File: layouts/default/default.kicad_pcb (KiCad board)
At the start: 2 copper layers, 39 x 17 mm, 13 parts

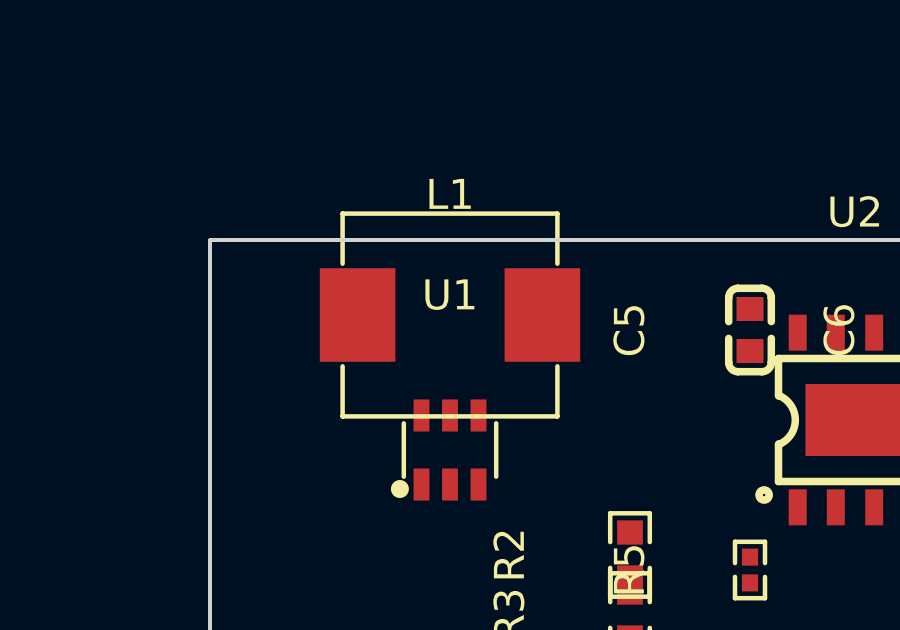
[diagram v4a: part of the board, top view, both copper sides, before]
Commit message: Use compact 4x4x2mm inductor (SMNR4020-22UH)
Replaced bulky 7.3x6.6x3mm inductor with 4x4x2mm shielded version.
Same 22µH value, 1.05A rated - sufficient for Pi Zero 2W load.
Max component height now 2.1mm (SS34 Schottky diode).
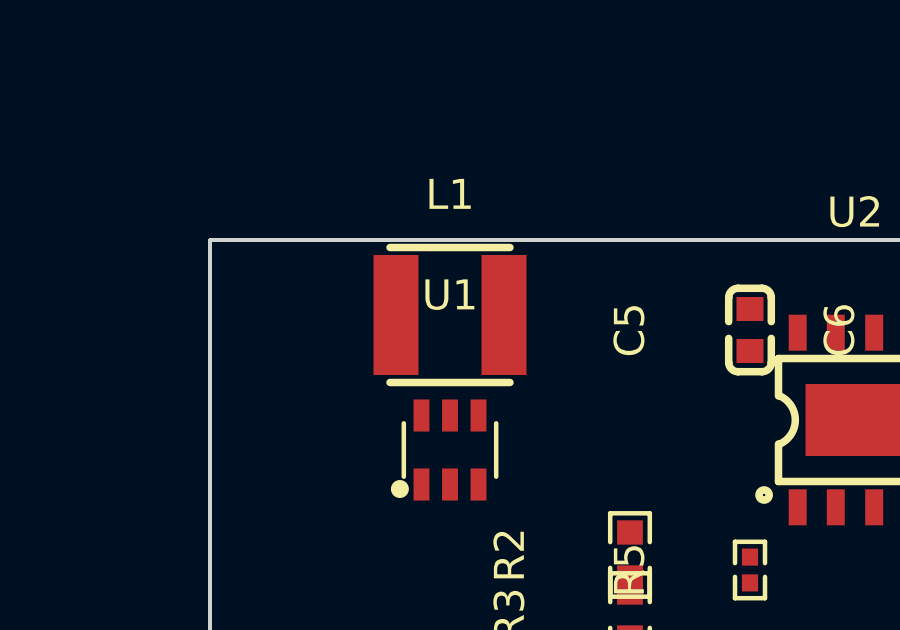
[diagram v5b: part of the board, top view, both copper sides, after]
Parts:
- L1: value L 0H -> (none); footprint SXN_SMMS0630_220M:IND-SMD_L7.3-W6.6_MHCI06030 -> SXN_SMNR4020_22UH:IND-SMD_L4.0-W4.0_LQH44PN2R2MP0L
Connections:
- D1 pad 2: A -> 2
- L1 pad 1: hv -> 2
- L1 pad 2: A -> hv
- U1 pad 1: A -> 2
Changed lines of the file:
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@@
 	(net 14 "c_out-power-hv")
 	(net 15 "lv")
-	(net 1 "A")
+	(net 1 "2")
 	(net 3 "hv")
 	(net 4 "FB")
@@
 			(size 0.53 1.07)
 			(layers "F.Cu" "F.Paste" "F.Mask")
-			(net 1 "A")
+			(net 1 "2")
 		)
 		(pad "2" smd rect
@@
 		)
 	)
-	(footprint "SXN_SMMS0630_220M:IND-SMD_L7.3-W6.6_MHCI06030"
+	(footprint "SXN_SMNR4020_22UH:IND-SMD_L4.0-W4.0_LQH44PN2R2MP0L"
 		(layer "F.Cu")
 		(at 107 82.5)
@@
 			)
 		)
-		(property "Value" "L 0H"
+		(property "Value" ""
 			(at 0 4)
 			(layer "F.Fab")
@@
 			)
 		)
-		(property "LCSC" "C128694"
-			(at 0 0 0)
-			(layer "User.9")
-			(hide yes)
-		)
-		(property "Manufacturer" "SXN(Shun Xiang Nuo Elec)"
+		(property "LCSC" "C135264"
+			(at 0 0 0)
+			(layer "User.9")
+			(hide yes)
+		)
+		(property "Manufacturer" "SXN"
 			(at 0 0 0)
 			(layer "User.9")
@@
 			(hide yes)
 		)
-		(property "Partnumber" "SMMS0630-220M"
-			(at 0 0 0)
-			(layer "User.9")
-			(hide yes)
-		)
-		(property "Datasheet" "https://www.lcsc.com/datasheet/lcsc_datasheet_2108131530_SXN-Shun-Xiang-Nuo-Elec-SMMS0630-220M_C128694.pdf"
+		(property "Partnumber" "SMNR4020-22UH"
+			(at 0 0 0)
+			(layer "User.9")
+			(hide yes)
+		)
+		(property "Datasheet" "https://www.lcsc.com/datasheet/lcsc_datasheet_2108131530_SXN-Shun-Xiang-Nuo-Elec-SMNR4020-22UH_C135264.pdf"
 			(at 0 0 0)
 			(layer "User.9")
@@
 			(hide yes)
 		)
-		(property "lcsc_id" "C128694"
+		(property "lcsc_id" "C135264"
 			(at 0 0 0)
 			(layer "User.9")
@@
 		(attr smd)
 		(fp_line
-			(start -3.58 -1.71)
-			(end -3.58 -3.38)
-			(stroke
-				(width 0.15)
-				(type solid)
-			)
-			(layer "F.SilkS")
-			(layers "F.SilkS")
-			(locked no)
-		)
-		(fp_line
-			(start -3.58 -3.38)
-			(end 3.58 -3.38)
-			(stroke
-				(width 0.15)
-				(type solid)
-			)
-			(layer "F.SilkS")
-			(layers "F.SilkS")
-			(locked no)
-		)
-		(fp_line
-			(start 3.58 -3.38)
-			(end 3.58 -1.71)
-			(stroke
-				(width 0.15)
-				(type solid)
-			)
-			(layer "F.SilkS")
-			(layers "F.SilkS")
-			(locked no)
-		)
-		(fp_line
-			(start -3.58 1.71)
-			(end -3.58 3.38)
-			(stroke
-				(width 0.15)
-				(type solid)
-			)
-			(layer "F.SilkS")
-			(layers "F.SilkS")
-			(locked no)
-		)
-		(fp_line
-			(start -3.58 3.38)
-			(end 3.58 3.38)
-			(stroke
-				(width 0.15)
-				(type solid)
-			)
-			(layer "F.SilkS")
-			(layers "F.SilkS")
-			(locked no)
-		)
-		(fp_line
-			(start 3.58 3.38)
-			(end 3.58 1.71)
-			(stroke
-				(width 0.15)
+			(start -2 -2.25)
+			(end 2 -2.25)
+			(stroke
+				(width 0.25)
+				(type solid)
+			)
+			(layer "F.SilkS")
+			(layers "F.SilkS")
+			(locked no)
+		)
+		(fp_line
+			(start -2 2.25)
+			(end 2 2.25)
+			(stroke
+				(width 0.25)
 				(type solid)
 			)
@@
 		)
 		(fp_circle
-			(center -3.55 3.31)
-			(end -3.52 3.31)
+			(center -2 2)
+			(end -1.97 2)
 			(stroke
 				(width 0.06)
@@
 			)
 		)
+		(pad "1" smd rect
+			(at -1.8 0 0)
+			(size 1.5 4)
+			(layers "F.Cu" "F.Paste" "F.Mask")
+			(net 1 "2")
+		)
 		(pad "2" smd rect
-			(at 3.08 0 0)
-			(size 2.52 3.12)
-			(layers "F.Cu" "F.Paste" "F.Mask")
-			(net 1 "A")
-		)
-		(pad "1" smd rect
-			(at -3.08 0 0)
-			(size 2.52 3.12)
+			(at 1.8 0 0)
+			(size 1.5 4)
 			(layers "F.Cu" "F.Paste" "F.Mask")
 			(net 3 "hv")
 		)
 		(embedded_fonts no)
-		(model "${KIPRJMOD}/../../parts/SXN_SMMS0630_220M/IND-SMD_L7.1-W6.6-H2.8.step"
+		(model "${KIPRJMOD}/../../parts/SXN_SMNR4020_22UH/IND-SMD_L4.0-W4.0-H1.65.STEP"
 			(offset
 				(xyz 0 0 -0)
@@
 			(size 2 2)
 			(layers "F.Cu" "F.Paste" "F.Mask")
-			(net 1 "A")
+			(net 1 "2")
 		)
 		(pad "1" smd rect

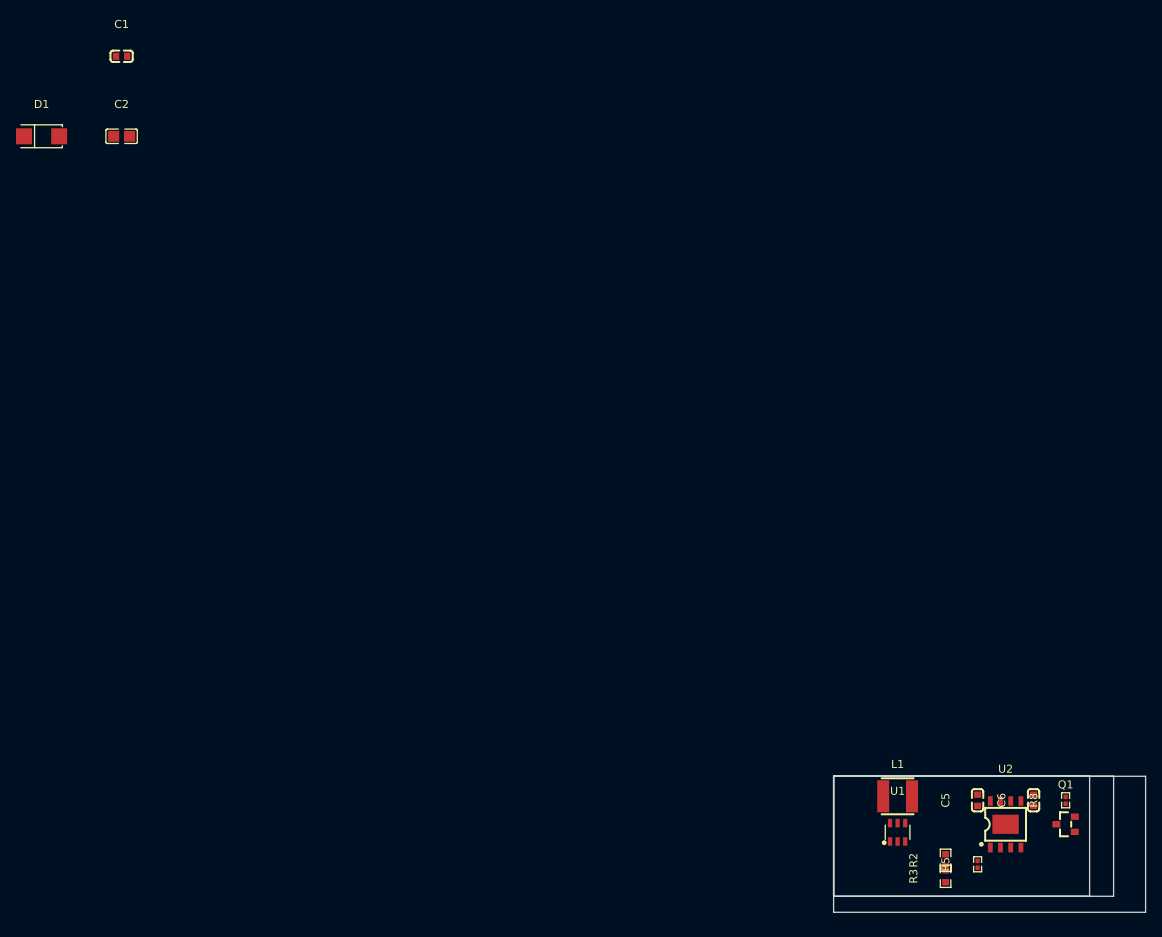
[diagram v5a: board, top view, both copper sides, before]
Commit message: Add PCB layout: 6 solder pads, component placement, routing, ground pour
- Created SolderPad component (2x1.5mm SMD pads) for 6 wire connections
- Board outline: 30x18mm with rounded corners
- 3-zone layout: charger (left) → MOSFET (center) → boost (right)
- Solder pads along bottom edge: VUSB, GND, VBAT, PI_EN, V5_PI, CHG
- 50 trace segments, 11 vias, GND pour on B.Cu
- Power traces 0.5mm, signal traces 0.25mm
- Silkscreen labels for all pads, board title NW-PWR
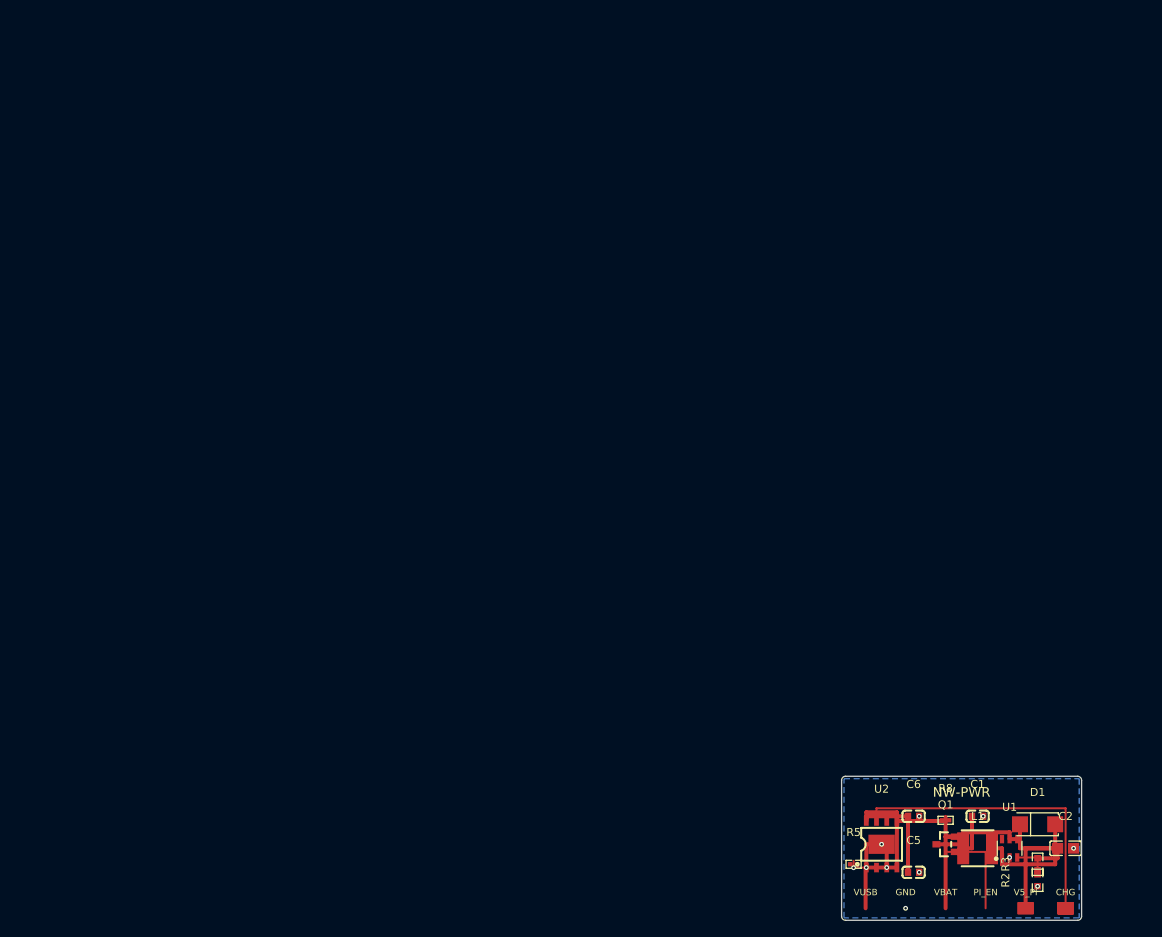
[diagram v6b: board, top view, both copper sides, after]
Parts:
- added J1, J3, J4, J5: , SolderPad:SolderPad, F.Cu at (128.0, 96.5)
- added J2, J6: , SolderPad:SolderPad, F.Cu at (123.0, 96.5)
- moved D1 151.3 mm to (124.5, 86.0)
- moved C2 147.8 mm to (128.0, 89.0)
- moved C1 143.1 mm to (117.0, 85.0)
- moved U2 15.7 mm to (105.0, 88.5)
- moved R5 15.5 mm to (101.5, 91.0), turned to 0 degrees
- moved Q1 15.2 mm to (113.0, 88.5)
- moved R8 15.2 mm to (113.0, 85.5), turned to 0 degrees
- moved C6 15.1 mm to (109.0, 85.0), turned to 0 degrees
- moved U1 14.1 mm to (121.0, 89.0)
- moved C5 12.0 mm to (109.0, 92.0), turned to 0 degrees
- moved L1 11.9 mm to (117.0, 89.0)
- moved R2 11.8 mm to (124.5, 93.0)
- moved R3 11.6 mm to (124.5, 91.0)
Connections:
- L1 pad 1: 2 -> hv
- L1 pad 2: hv -> 2
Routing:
- net chg_stat: track 0.00 -> 37.7 mm
- net c_in-power-hv: track 0.00 -> 26.6 mm
- net c_bat-power-hv: track 0.00 -> 26.2 mm
- net c_out-power-hv: track 0.00 -> 23.0 mm
- net hv: track 0.00 -> 18.5 mm
- net pi_en: track 0.00 -> 15.6 mm
- net 2: track 0.00 -> 14.9 mm
- net lv: track 0.00 -> 8.37 mm, vias 0 -> 11
- net FB: track 0.00 -> 4.65 mm
- net PROG: track 0.00 -> 3.70 mm
- added copper zone on B.Cu, net lv
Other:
- board size 39 x 17 mm -> 30 x 18 mm
- board text added: "CHG"
- board text added: "GND"
- board text added: "NW-PWR"
- board text added: "PI_EN"
- board text added: "V5_PI"
- board text added: "VBAT"
- board text added: "VUSB"

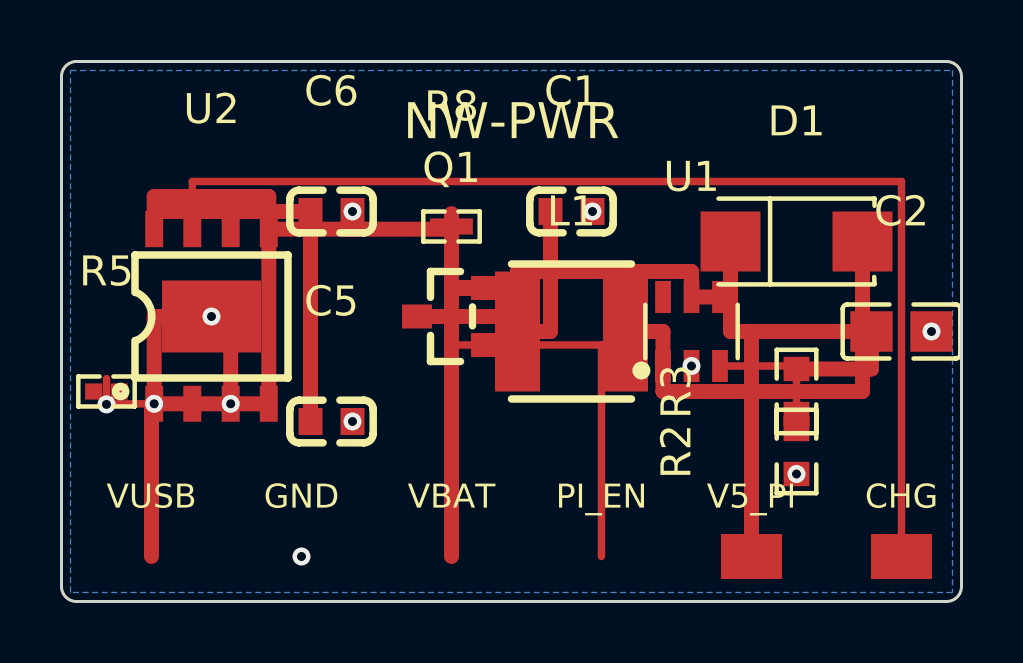
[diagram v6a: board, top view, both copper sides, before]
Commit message: Fix layout: proper pad spacing, clean placement, remove bad routing
- 6 solder pads evenly spaced along bottom edge (4.8mm apart)
- Components grouped: charger left, MOSFET center, boost right
- Removed all programmatic traces/vias/zones - route in KiCad
- Clean silkscreen labels (VUSB, GND, VBAT, EN, 5V, CHG)
- 30x18mm board outline
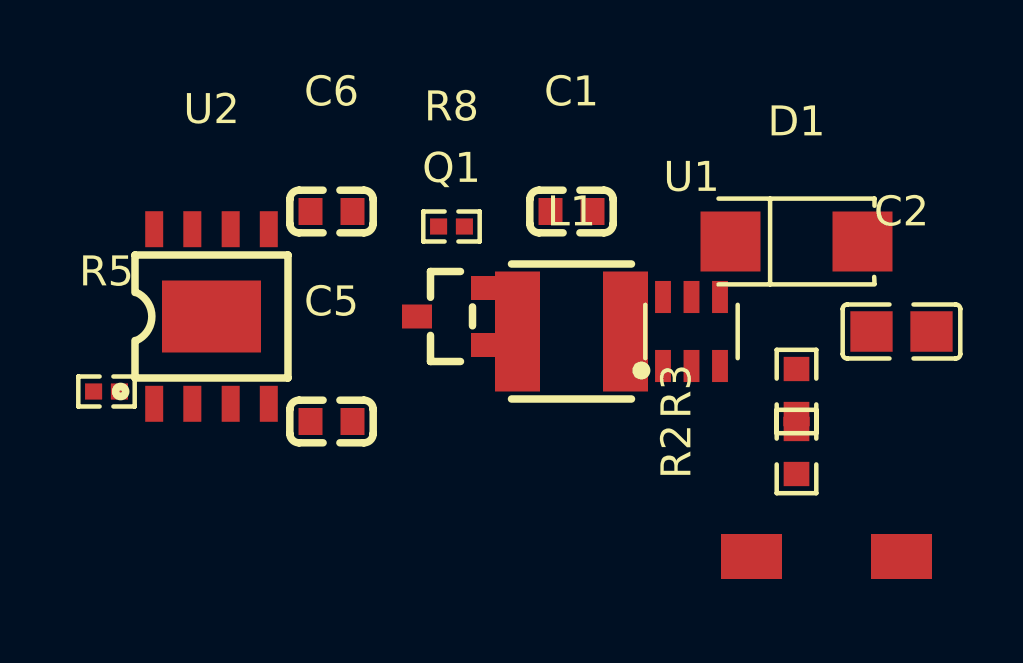
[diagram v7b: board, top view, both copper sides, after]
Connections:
- C1 pad 2: lv -> (no net)
- C2 pad 2: lv -> (no net)
- C5 pad 2: lv -> (no net)
- C6 pad 2: lv -> (no net)
- J2 pad 1: lv -> (no net)
- R2 pad 2: lv -> (no net)
- R5 pad 2: lv -> (no net)
- U1 pad 2: lv -> (no net)
- U2 pad 1: lv -> (no net)
- U2 pad 3: lv -> (no net)
- U2 pad 9: lv -> (no net)
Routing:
- net chg_stat: track 37.7 -> 0.00 mm
- net c_in-power-hv: track 26.6 -> 0.00 mm
- net c_bat-power-hv: track 26.2 -> 0.00 mm
- net c_out-power-hv: track 23.0 -> 0.00 mm
- net hv: track 18.5 -> 0.00 mm
- net pi_en: track 15.6 -> 0.00 mm
- net 2: track 14.9 -> 0.00 mm
- net lv: track 8.37 -> 0.00 mm, vias 11 -> 0
- net FB: track 4.65 -> 0.00 mm
- net PROG: track 3.70 -> 0.00 mm
- removed copper zone on B.Cu, net lv
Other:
- board outline removed
- board text removed: "CHG"
- board text removed: "GND"
- board text removed: "NW-PWR"
- board text removed: "PI_EN"
- board text removed: "V5_PI"
- board text removed: "VBAT"
- board text removed: "VUSB"

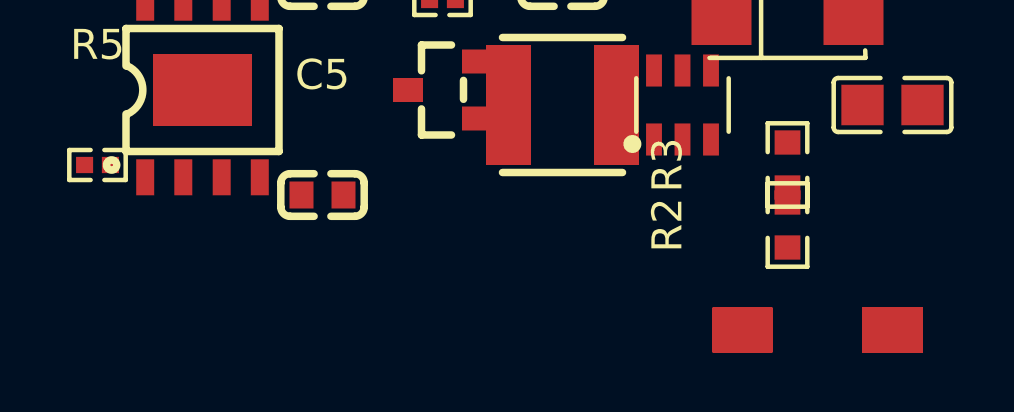
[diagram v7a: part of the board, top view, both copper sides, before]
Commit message: Fix all 6 solder pad positions (were stacked, now spaced)
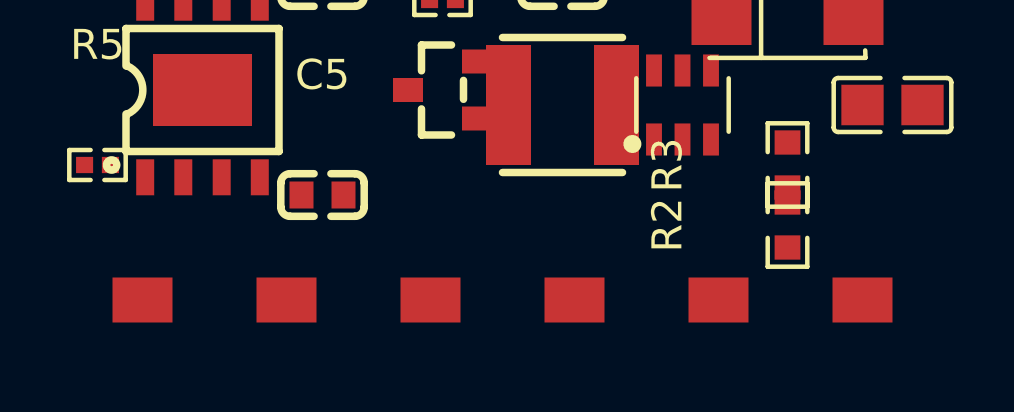
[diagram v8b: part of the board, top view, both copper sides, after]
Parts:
- moved J6 20.0 mm to (103.0, 95.5)
- moved J5 15.4 mm to (112.6, 95.5)
- moved J2 15.2 mm to (107.8, 95.5)
- moved J3 10.6 mm to (117.4, 95.5)
- moved J4 5.89 mm to (122.2, 95.5)
- moved J1 1.41 mm to (127.0, 95.5)
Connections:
- C1 pad 2: (no net) -> lv
- C2 pad 2: (no net) -> lv
- C5 pad 2: (no net) -> lv
- C6 pad 2: (no net) -> lv
- J2 pad 1: (no net) -> lv
- R2 pad 2: (no net) -> lv
- R5 pad 2: (no net) -> lv
- U1 pad 2: (no net) -> lv
- U2 pad 1: (no net) -> lv
- U2 pad 3: (no net) -> lv
- U2 pad 9: (no net) -> lv
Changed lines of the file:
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@@
 	(net 7 "c_bat-power-hv")
 	(net 8 "pi_en")
+	(net 11 "lv")
 	(footprint "TOPPOWER_TP4056_42_ESOP8:ESOP-8_L4.9-W3.9-P1.27-LS6.0-BL-EP"
 		(layer "F.Cu")
@@
 			(size 0.6 1.2)
 			(layers "F.Cu" "F.Paste" "F.Mask")
-			(net 0 "")
+			(net 11 "lv")
 		)
 		(pad "2" smd rect
@@
 			(size 0.6 1.2)
 			(layers "F.Cu" "F.Paste" "F.Mask")
-			(net 0 "")
+			(net 11 "lv")
 		)
 		(pad "4" smd rect
@@
 			(size 3.3 2.4)
 			(layers "F.Cu" "F.Paste" "F.Mask")
-			(net 0 "")
+			(net 11 "lv")
 		)
 		(embedded_fonts no)
@@
 			(size 0.53 1.07)
 			(layers "F.Cu" "F.Paste" "F.Mask")
-			(net 0 "")
+			(net 11 "lv")
 		)
 		(pad "3" smd rect
@@
 			(size 0.8 0.9)
 			(layers "F.Cu" "F.Paste" "F.Mask")
-			(net 0 "")
+			(net 11 "lv")
 		)
 		(pad "1" smd rect
@@
 			(size 0.8 0.9)
 			(layers "F.Cu" "F.Paste" "F.Mask")
-			(net 0 "")
+			(net 11 "lv")
 		)
 		(pad "1" smd rect
@@
 			(size 0.57 0.54)
 			(layers "F.Cu" "F.Paste" "F.Mask")
-			(net 0 "")
+			(net 11 "lv")
 		)
 		(pad "1" smd rect
@@
 			(size 0.81 0.86)
 			(layers "F.Cu" "F.Paste" "F.Mask")
-			(net 0 "")
+			(net 11 "lv")
 		)
 		(pad "1" smd rect
@@
 			(size 1.41 1.35)
 			(layers "F.Cu" "F.Paste" "F.Mask")
-			(net 0 "")
+			(net 11 "lv")
 		)
 		(pad "1" smd rect
@@
 			(size 0.8 0.9)
 			(layers "F.Cu" "F.Paste" "F.Mask")
-			(net 0 "")
+			(net 11 "lv")
 		)
 		(pad "1" smd rect
@@
 	(footprint "SolderPad:SolderPad"
 		(layer "F.Cu")
-		(at 123 96.5)
+		(at 103 95.5)
 		(property "LCSC" "NA"
 			(at 0 0 0)
@@
 	(footprint "SolderPad:SolderPad"
 		(layer "F.Cu")
-		(at 123 96.5)
+		(at 107.8 95.5)
 		(property "LCSC" "NA"
 			(at 0 0 0)
@@
 			(size 2 1.5)
 			(layers "F.Cu" "F.Paste" "F.Mask")
-			(net 0 "")
+			(net 11 "lv")
 		)
 	)
 	(footprint "SolderPad:SolderPad"
 		(layer "F.Cu")
-		(at 128 96.5)
+		(at 112.6 95.5)
 		(property "LCSC" "NA"
 			(at 0 0 0)
@@
 	(footprint "SolderPad:SolderPad"
 		(layer "F.Cu")
-		(at 128 96.5)
+		(at 122.2 95.5)
 		(property "LCSC" "NA"
 			(at 0 0 0)
@@
 	(footprint "SolderPad:SolderPad"
 		(layer "F.Cu")
-		(at 128 96.5)
+		(at 117.4 95.5)
 		(property "LCSC" "NA"
 			(at 0 0 0)
@@
 	(footprint "SolderPad:SolderPad"
 		(layer "F.Cu")
-		(at 128 96.5)
+		(at 127 95.5)
 		(property "LCSC" "NA"
 			(at 0 0 0)
